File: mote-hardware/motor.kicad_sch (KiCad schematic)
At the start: 10 parts, among them J7 JST_PH_B6B, J8 JST_PH_B6B, U5 DRV8833PW

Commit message: Hardware v0.0.0 order (#36)
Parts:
- C19: LCSC (none) -> C15195
- C2: value 100uF -> 100u; LCSC (none) -> C15008
- C20: LCSC (none) -> C12530
- C21: value 10uF -> 10u; LCSC (none) -> C440198
- C22: value 0.1uF -> 0.1u; LCSC (none) -> C1525
- J7, J8: LCSC (none) -> C495261
- R11, R12: LCSC (none) -> C7467478
- U5: LCSC (none) -> C50506
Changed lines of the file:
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@@
 			)
 		)
-		(property "Value" "100uF"
+		(property "Value" "100u"
 			(at 167.386 70.358 0)
 			(effects
@@
 		)
 		(property "Description" "Unpolarized capacitor"
+			(at 166.37 67.31 0)
+			(effects
+				(font
+					(size 1.27 1.27)
+				)
+				(hide yes)
+			)
+		)
+		(property "LCSC" "C15008"
+			(at 166.37 67.31 0)
+			(effects
+				(font
+					(size 1.27 1.27)
+				)
+				(hide yes)
+			)
+		)
+		(property "JLCPCB_CORRECTION" ""
 			(at 166.37 67.31 0)
 			(effects
@@
 			)
 		)
-		(property "Value" "10uF"
+		(property "Value" "10u"
 			(at 181.61 69.85 0)
 			(effects
@@
 		)
 		(property "Description" "Unpolarized capacitor"
+			(at 180.34 67.31 0)
+			(effects
+				(font
+					(size 1.27 1.27)
+				)
+				(hide yes)
+			)
+		)
+		(property "LCSC" "C440198"
+			(at 180.34 67.31 0)
+			(effects
+				(font
+					(size 1.27 1.27)
+				)
+				(hide yes)
+			)
+		)
+		(property "JLCPCB_CORRECTION" ""
 			(at 180.34 67.31 0)
 			(effects
@@
 			)
 		)
-		(property "Value" "0.1uF"
+		(property "Value" "0.1u"
 			(at 194.056 70.104 0)
 			(effects
@@
 		)
 		(property "Description" "Unpolarized capacitor"
+			(at 193.04 67.31 0)
+			(effects
+				(font
+					(size 1.27 1.27)
+				)
+				(hide yes)
+			)
+		)
+		(property "LCSC" "C1525"
+			(at 193.04 67.31 0)
+			(effects
+				(font
+					(size 1.27 1.27)
+				)
+				(hide yes)
+			)
+		)
+		(property "JLCPCB_CORRECTION" ""
 			(at 193.04 67.31 0)
 			(effects
@@
 			)
 		)
+		(property "LCSC" "C495261"
+			(at 198.12 125.73 0)
+			(effects
+				(font
+					(size 1.27 1.27)
+				)
+				(hide yes)
+			)
+		)
+		(property "JLCPCB_CORRECTION" ""
+			(at 198.12 125.73 0)
+			(effects
+				(font
+					(size 1.27 1.27)
+				)
+				(hide yes)
+			)
+		)
 		(pin "3"
 		)
@@
 			)
 		)
+		(property "LCSC" "C495261"
+			(at 198.12 104.14 0)
+			(effects
+				(font
+					(size 1.27 1.27)
+				)
+				(hide yes)
+			)
+		)
+		(property "JLCPCB_CORRECTION" ""
+			(at 198.12 104.14 0)
+			(effects
+				(font
+					(size 1.27 1.27)
+				)
+				(hide yes)
+			)
+		)
 		(pin "3"
 		)
@@
 		(property "Description" "Resistor"
 			(at 127 104.14 0)
+			(effects
+				(font
+					(size 1.27 1.27)
+				)
+				(hide yes)
+			)
+		)
+		(property "LCSC" "C7467478"
+			(at 127 104.14 90)
+			(effects
+				(font
+					(size 1.27 1.27)
+				)
+				(hide yes)
+			)
+		)
+		(property "JLCPCB_CORRECTION" ""
+			(at 127 104.14 90)
 			(effects
 				(font
@@
 			)
 		)
+		(property "LCSC" "C50506"
+			(at 152.4 106.68 0)
+			(effects
+				(font
+					(size 1.27 1.27)
+				)
+				(hide yes)
+			)
+		)
+		(property "JLCPCB_CORRECTION" ""
+			(at 152.4 106.68 0)
+			(effects
+				(font
+					(size 1.27 1.27)
+				)
+				(hide yes)
+			)
+		)
 		(pin "10"
 		)
@@
 			)
 		)
+		(property "LCSC" "C15195"
+			(at 138.43 81.28 0)
+			(effects
+				(font
+					(size 1.27 1.27)
+				)
+				(hide yes)
+			)
+		)
+		(property "JLCPCB_CORRECTION" ""
+			(at 138.43 81.28 0)
+			(effects
+				(font
+					(size 1.27 1.27)
+				)
+				(hide yes)
+			)
+		)
 		(pin "2"
 		)
@@
 		(property "Description" "Resistor"
 			(at 127 101.6 0)
+			(effects
+				(font
+					(size 1.27 1.27)
+				)
+				(hide yes)
+			)
+		)
+		(property "LCSC" "C7467478"
+			(at 127 101.6 90)
+			(effects
+				(font
+					(size 1.27 1.27)
+				)
+				(hide yes)
+			)
+		)
+		(property "JLCPCB_CORRECTION" ""
+			(at 127 101.6 90)
 			(effects
 				(font
@@
 			(at 168.91 88.9 0)
 			(effects
+				(font
+					(size 1.27 1.27)
+				)
+				(hide yes)
+			)
+		)
+		(property "LCSC" "C12530"
+			(at 168.91 88.9 0)
+			(effects
+				(font
+					(size 1.27 1.27)
+				)
+				(hide yes)
+			)
+		)
+		(property "JLCPCB_CORRECTION" ""
+			(at 168.91 88.9 0)
+			(effects

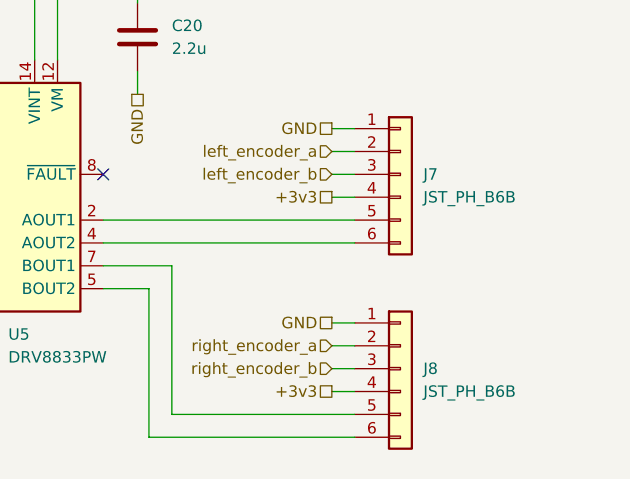
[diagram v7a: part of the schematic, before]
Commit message: Add comments to schematic, respect ground pin on SWD and UART connectors
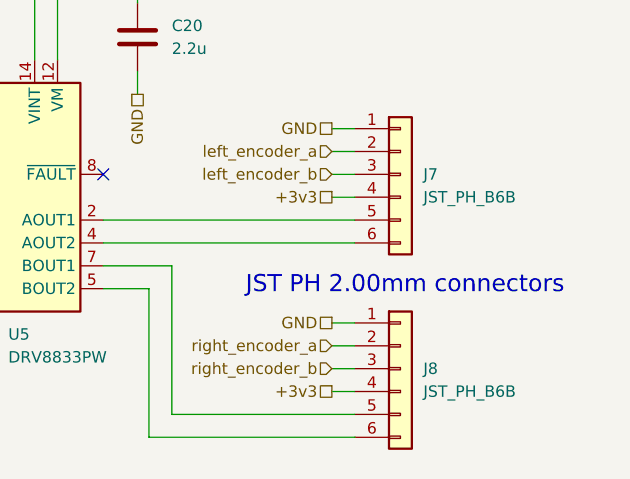
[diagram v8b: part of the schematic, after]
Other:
- note added: "JST PH 2.00mm connectors"
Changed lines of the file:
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@@
 		(company "github.com/empriselab/mote-core")
+	)
+	(text "JST PH 2.00mm connectors"
+		(exclude_from_sim no)
+		(at 198.628 117.602 0)
+		(effects
+			(font
+				(size 1.905 1.905)
+			)
+			(justify bottom)
+		)
 	)
 	(text "1A current limit\n[CHOP = (0.2V / RSENSE)]"
